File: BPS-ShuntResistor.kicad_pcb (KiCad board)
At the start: 2 copper layers, 40.1 x 35.1 mm, 11 parts, among them J3 Amp_Conn

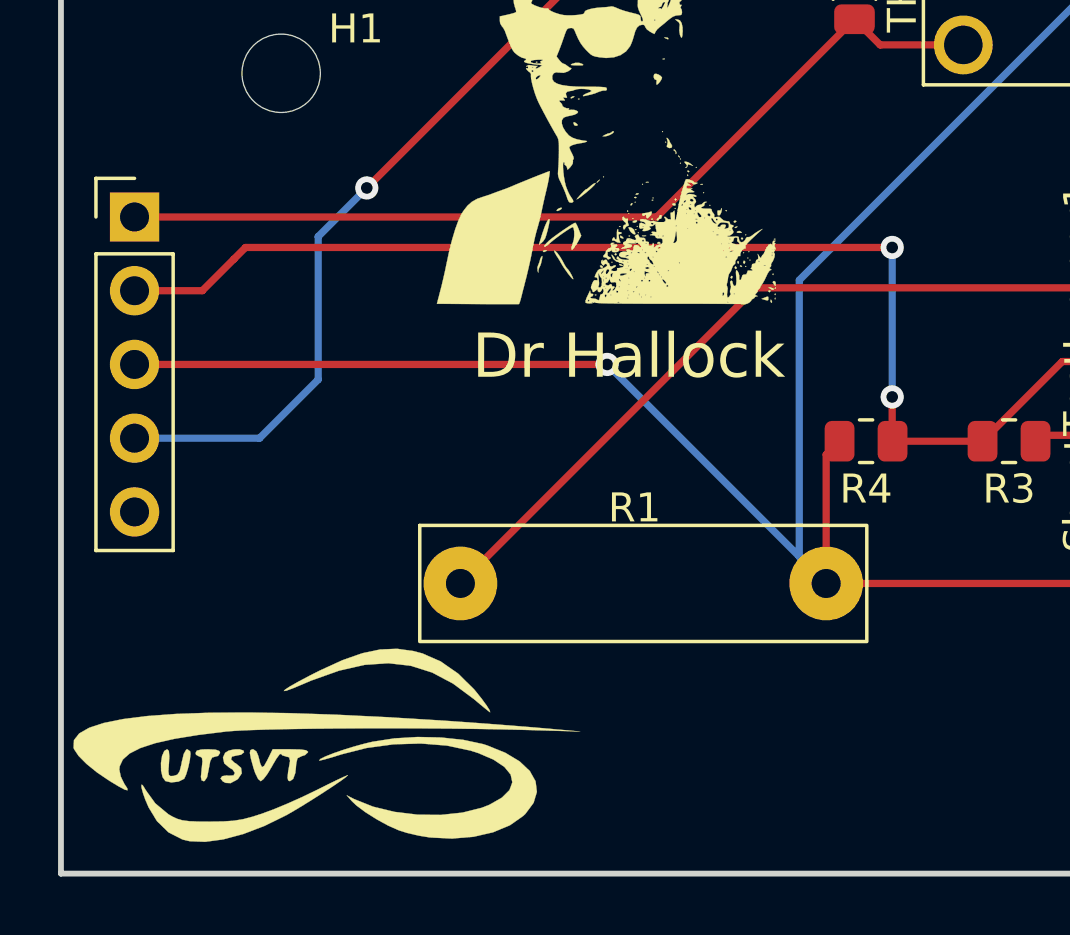
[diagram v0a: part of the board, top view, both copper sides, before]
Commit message: Fixed RSHL/RSHH connectors
Net labels were in wrong spot on circuit
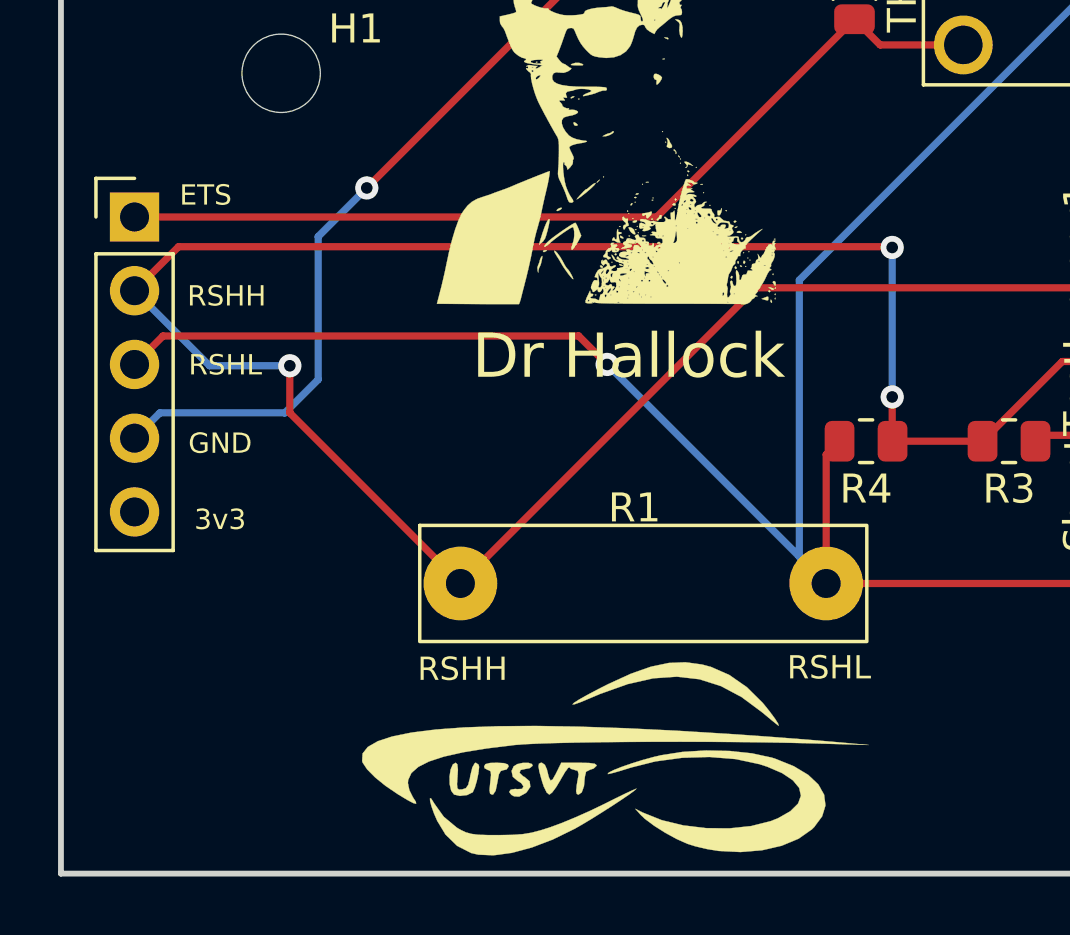
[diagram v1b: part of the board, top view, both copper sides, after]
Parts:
- moved LOGO1 9.95 mm to (127.3, 108.8)
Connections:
- J3 pad 2: RSHH -> Net-(J3-Pad2)
- R1 pad 1: Net-(R1-Pad1) -> RSHH
- R3 pad 2: RSHH -> Net-(J3-Pad2)
- R4 pad 1: RSHH -> Net-(J3-Pad2)
- ShuntTestJumper1 pad 2: Net-(R1-Pad1) -> RSHH
- ShuntTestJumper1 pad 3: RSHH -> Net-(J3-Pad2)
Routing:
- net Net-(J3-Pad2): track 0.00 -> 55.9 mm, vias 0 -> 2
- net Net-(R1-Pad1): track 28.1 -> 0.00 mm
- net RSHH: track 55.9 -> 44.4 mm, vias 2 -> 1
- net RSHL: track 71.7 -> 72.5 mm
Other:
- board text added: "3v3"
- board text added: "ETS"
- board text added: "GND"
- board text added: "RSHH"
- board text added: "RSHL"
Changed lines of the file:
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@@
   (net 5 "+3V3")
   (net 6 "/TestIn")
-  (net 7 "Net-(R1-Pad1)")
+  (net 7 "Net-(J3-Pad2)")
   (net 8 "unconnected-(ShuntTestJumper1-Pad1)")
   (footprint "Connector_PinHeader_2.54mm:PinHeader_1x05_P2.54mm_Vertical" (layer "F.Cu")
@@
   )
   (footprint "UTSVT_Special:UTSVT_Logo_Symbol" (layer "F.Cu")
-    (at 117.359054 108.285857)
+    (at 127.3 108.75)
     (property "Sheetfile" "BPS-ShuntResistor.kicad_sch")
     (property "Sheetname" "")
@@
       (net 6 "/TestIn") (pintype "passive"))
     (pad "2" smd roundrect (at 0.9125 0 180) (size 1.025 1.4) (layers "F.Cu" "F.Paste" "F.Mask") (roundrect_rratio 0.243902439)
-      (net 2 "RSHH") (pintype "passive"))
+      (net 7 "Net-(J3-Pad2)") (pintype "passive"))
     (model "${KICAD6_3DMODEL_DIR}/Resistor_SMD.3dshapes/R_0805_2012Metric.wrl"
       (offset (xyz 0 0 0))
@@
       (net 8 "unconnected-(ShuntTestJumper1-Pad1)") (pinfunction "Pin_1") (pintype "passive+no_connect"))
     (pad "2" thru_hole oval (at 0 2.54) (size 1.7 1.7) (drill 1) (layers *.Cu *.Mask)
-      (net 7 "Net-(R1-Pad1)") (pinfunction "Pin_2") (pintype "passive"))
+      (net 2 "RSHH") (pinfunction "Pin_2") (pintype "passive"))
     (pad "3" thru_hole oval (at 0 5.08) (size 1.7 1.7) (drill 1) (layers *.Cu *.Mask)
-      (net 2 "RSHH") (pinfunction "Pin_3") (pintype "passive"))
+      (net 7 "Net-(J3-Pad2)") (pinfunction "Pin_3") (pintype "passive"))
     (pad "4" thru_hole oval (at 0 7.62) (size 1.7 1.7) (drill 1) (layers *.Cu *.Mask)
       (net 6 "/TestIn") (pinfunction "Pin_4") (pintype "passive"))
@@
     (fp_line (start 1 0.625) (end -1 0.625) (layer "F.Fab") (width 0.1))
     (pad "1" smd roundrect (at -0.9125 0 180) (size 1.025 1.4) (layers "F.Cu" "F.Paste" "F.Mask") (roundrect_rratio 0.243902439)
-      (net 2 "RSHH") (pintype "passive"))
+      (net 7 "Net-(J3-Pad2)") (pintype "passive"))
     (pad "2" smd roundrect (at 0.9125 0 180) (size 1.025 1.4) (layers "F.Cu" "F.Paste" "F.Mask") (roundrect_rratio 0.243902439)
       (net 3 "RSHL") (pintype "passive"))
@@
       (net 1 "ETS") (pinfunction "Pin_1") (pintype "passive"))
     (pad "2" thru_hole circle (at 3 2) (size 2.028 2.028) (drill 1.328) (layers *.Cu *.Mask)
-      (net 2 "RSHH") (pinfunction "Pin_2") (pintype "passive"))
+      (net 7 "Net-(J3-Pad2)") (pinfunction "Pin_2") (pintype "passive"))
     (pad "3" thru_hole circle (at 3 -1.548) (size 2.028 2.028) (drill 1.328) (layers *.Cu *.Mask)
       (net 3 "RSHL") (pinfunction "Pin_3") (pintype "passive"))
@@
     (fp_rect (start -7.4 -2) (end 8 2) (layer "F.SilkS") (width 0.12) (fill none))
     (pad "1" thru_hole circle (at -6 0) (size 2.54 2.54) (drill 1) (layers *.Cu *.Mask)
-      (net 7 "Net-(R1-Pad1)") (pintype "passive"))
+      (net 2 "RSHH") (pintype "passive"))
     (pad "2" thru_hole circle (at 6.6 0) (size 2.54 2.54) (drill 1) (layers *.Cu *.Mask)
       (net 3 "RSHL") (pintype "passive"))
   )
   (gr_rect (start 108.49 77.47) (end 148.59 112.57) (layer "Edge.Cuts") (width 0.2) (fill none))
+  (gr_text "RSHL" (at 134.95 105.475) (layer "F.SilkS")
+    (effects (font (size 0.8 0.8) (thickness 0.2)))
+  )
+  (gr_text "3v3" (at 113.975 100.375) (layer "F.SilkS")
+    (effects (font (size 0.7 0.7) (thickness 0.175)))
+  )
+  (gr_text "ETS" (at 113.475 89.2) (layer "F.SilkS")
+    (effects (font (size 0.7 0.7) (thickness 0.175)))
+  )
+  (gr_text "RSHL" (at 114.15 95.05) (layer "F.SilkS")
+    (effects (font (size 0.7 0.7) (thickness 0.175)))
+  )
+  (gr_text "GND" (at 113.975 97.75) (layer "F.SilkS")
+    (effects (font (size 0.7 0.7) (thickness 0.175)))
+  )
+  (gr_text "RSHH\n" (at 122.325 105.525) (layer "F.SilkS")
+    (effects (font (size 0.8 0.8) (thickness 0.2)))
+  )
+  (gr_text "RSHH" (at 114.2 92.675) (layer "F.SilkS")
+    (effects (font (size 0.7 0.7) (thickness 0.175)))
+  )
   (gr_text "The connectors are aligned according to the\nBPS/Amperes board measurements" (at 90.925 65.175) (layer "Cmts.User")
     (effects (font (size 1.5 1.5) (thickness 0.3)))
@@
   (segment (start 136.7105 84.023) (end 135.825 83.1375) (width 0.25) (layer "F.Cu") (net 1))
   (segment (start 129.0125 89.95) (end 135.825 83.1375) (width 0.25) (layer "F.Cu") (net 1))
-  (segment (start 140.2375 97.675) (end 137.1375 97.675) (width 0.25) (layer "F.Cu") (net 2))
-  (segment (start 111.025 92.49) (end 113.36 92.49) (width 0.25) (layer "F.Cu") (net 2))
-  (segment (start 137.125 96.15) (end 137.125 97.6625) (width 0.25) (layer "F.Cu") (net 2))
-  (segment (start 114.85 91) (end 137.125 91) (width 0.25) (layer "F.Cu") (net 2))
-  (segment (start 140.2375 97.675) (end 142.9825 94.93) (width 0.25) (layer "F.Cu") (net 2))
-  (segment (start 113.36 92.49) (end 114.45 91.4) (width 0.25) (layer "F.Cu") (net 2))
-  (segment (start 114.45 91.4) (end 114.85 91) (width 0.25) (layer "F.Cu") (net 2))
-  (segment (start 142.9825 94.93) (end 146.1 94.93) (width 0.25) (layer "F.Cu") (net 2))
-  (segment (start 137.125 97.6625) (end 137.1375 97.675) (width 0.25) (layer "F.Cu") (net 2))
-  (via (at 137.125 96.15) (size 0.8) (drill 0.4) (layers "F.Cu" "B.Cu") (net 2))
-  (via (at 137.125 91) (size 0.8) (drill 0.4) (layers "F.Cu" "B.Cu") (net 2))
-  (segment (start 137.125 91) (end 137.125 96.15) (width 0.25) (layer "B.Cu") (net 2))
-  (segment (start 145.575 84.023) (end 144.025 85.573) (width 0.25) (layer "B.Cu") (net 2))
-  (segment (start 144.025 92.855) (end 146.1 94.93) (width 0.25) (layer "B.Cu") (net 2))
-  (segment (start 144.025 85.573) (end 144.025 92.855) (width 0.25) (layer "B.Cu") (net 2))
+  (segment (start 122.25 102.575) (end 116.375 96.7) (width 0.25) (layer "F.Cu") (net 2))
+  (segment (start 116.375 96.7) (end 116.375 95.075) (width 0.25) (layer "F.Cu") (net 2))
+  (segment (start 146.1 92.39) (end 132.435 92.39) (width 0.25) (layer "F.Cu") (net 2))
+  (segment (start 132.435 92.39) (end 122.25 102.575) (width 0.25) (layer "F.Cu") (net 2))
+  (via (at 116.375 95.075) (size 0.8) (drill 0.4) (layers "F.Cu" "B.Cu") (net 2))
+  (segment (start 113.61 95.075) (end 111.025 92.49) (width 0.25) (layer "B.Cu") (net 2))
+  (segment (start 116.375 95.075) (end 113.61 95.075) (width 0.25) (layer "B.Cu") (net 2))
+  (segment (start 111.025 95.03) (end 112.005 94.05) (width 0.25) (layer "F.Cu") (net 3))
   (segment (start 134.85 98.1375) (end 134.85 102.575) (width 0.25) (layer "F.Cu") (net 3))
+  (segment (start 126.325 94.05) (end 127.305 95.03) (width 0.25) (layer "F.Cu") (net 3))
   (segment (start 146.1 100.01) (end 143.535 102.575) (width 0.25) (layer "F.Cu") (net 3))
+  (segment (start 112.005 94.05) (end 126.325 94.05) (width 0.25) (layer "F.Cu") (net 3))
   (segment (start 143.535 102.575) (end 134.85 102.575) (width 0.25) (layer "F.Cu") (net 3))
   (segment (start 135.3125 97.675) (end 134.85 98.1375) (width 0.25) (layer "F.Cu") (net 3))
-  (segment (start 111.025 95.03) (end 127.305 95.03) (width 0.25) (layer "F.Cu") (net 3))
   (via (at 127.305 95.03) (size 0.8) (drill 0.4) (layers "F.Cu" "B.Cu") (net 3))
   (segment (start 145.575 80.475) (end 133.925 92.125) (width 0.25) (layer "B.Cu") (net 3))
@@
   (segment (start 136.6625 80.475) (end 135.825 81.3125) (width 0.25) (layer "F.Cu") (net 4))
   (via (at 119.025 88.95) (size 0.8) (drill 0.4) (layers "F.Cu" "B.Cu") (net 4))
-  (segment (start 115.325 97.575) (end 115.32 97.57) (width 0.25) (layer "B.Cu") (net 4))
-  (segment (start 115.32 97.57) (end 111.025 97.57) (width 0.25) (layer "B.Cu") (net 4))
-  (segment (start 117.35 95.55) (end 115.325 97.575) (width 0.25) (layer "B.Cu") (net 4))
-  (segment (start 117.35 90.625) (end 117.35 95.55) (width 0.25) (layer "B.Cu") (net 4))
   (segment (start 119.025 88.95) (end 117.35 90.625) (width 0.25) (layer "B.Cu") (net 4))
+  (segment (start 117.35 90.625) (end 117.35 95.55) (width 0.25) (layer "B.Cu") (net 4))
+  (segment (start 117.35 95.55) (end 116.2 96.7) (width 0.25) (layer "B.Cu") (net 4))
+  (segment (start 111.895 96.7) (end 111.025 97.57) (width 0.25) (layer "B.Cu") (net 4))
+  (segment (start 116.2 96.7) (end 111.895 96.7) (width 0.25) (layer "B.Cu") (net 4))
   (segment (start 142.2675 97.47) (end 146.1 97.47) (width 0.25) (layer "F.Cu") (net 6))
   (segment (start 142.0625 97.675) (end 142.2675 97.47) (width 0.25) (layer "F.Cu") (net 6))
-  (segment (start 146.1 92.39) (end 132.435 92.39) (width 0.25) (layer "F.Cu") (net 7))
-  (segment (start 132.435 92.39) (end 122.25 102.575) (width 0.25) (layer "F.Cu") (net 7))
+  (segment (start 140.2375 97.675) (end 137.1375 97.675) (width 0.25) (layer "F.Cu") (net 7))
+  (segment (start 137.125 96.15) (end 137.125 97.6625) (width 0.25) (layer "F.Cu") (net 7))
+  (segment (start 112.54 90.975) (end 137.1 90.975) (width 0.25) (layer "F.Cu") (net 7))
+  (segment (start 140.2375 97.675) (end 142.9825 94.93) (width 0.25) (layer "F.Cu") (net 7))
+  (segment (start 142.9825 94.93) (end 146.1 94.93) (width 0.25) (layer "F.Cu") (net 7))
+  (segment (start 137.1 90.975) (end 137.125 91) (width 0.25) (layer "F.Cu") (net 7))
+  (segment (start 111.025 92.49) (end 112.54 90.975) (width 0.25) (layer "F.Cu") (net 7))
+  (segment (start 137.125 97.6625) (end 137.1375 97.675) (width 0.25) (layer "F.Cu") (net 7))
+  (via (at 137.125 96.15) (size 0.8) (drill 0.4) (layers "F.Cu" "B.Cu") (net 7))
+  (via (at 137.125 91) (size 0.8) (drill 0.4) (layers "F.Cu" "B.Cu") (net 7))
+  (segment (start 137.125 91) (end 137.125 96.15) (width 0.25) (layer "B.Cu") (net 7))
+  (segment (start 145.575 84.023) (end 144.025 85.573) (width 0.25) (layer "B.Cu") (net 7))
+  (segment (start 144.025 92.855) (end 146.1 94.93) (width 0.25) (layer "B.Cu") (net 7))
+  (segment (start 144.025 85.573) (end 144.025 92.855) (width 0.25) (layer "B.Cu") (net 7))
 )

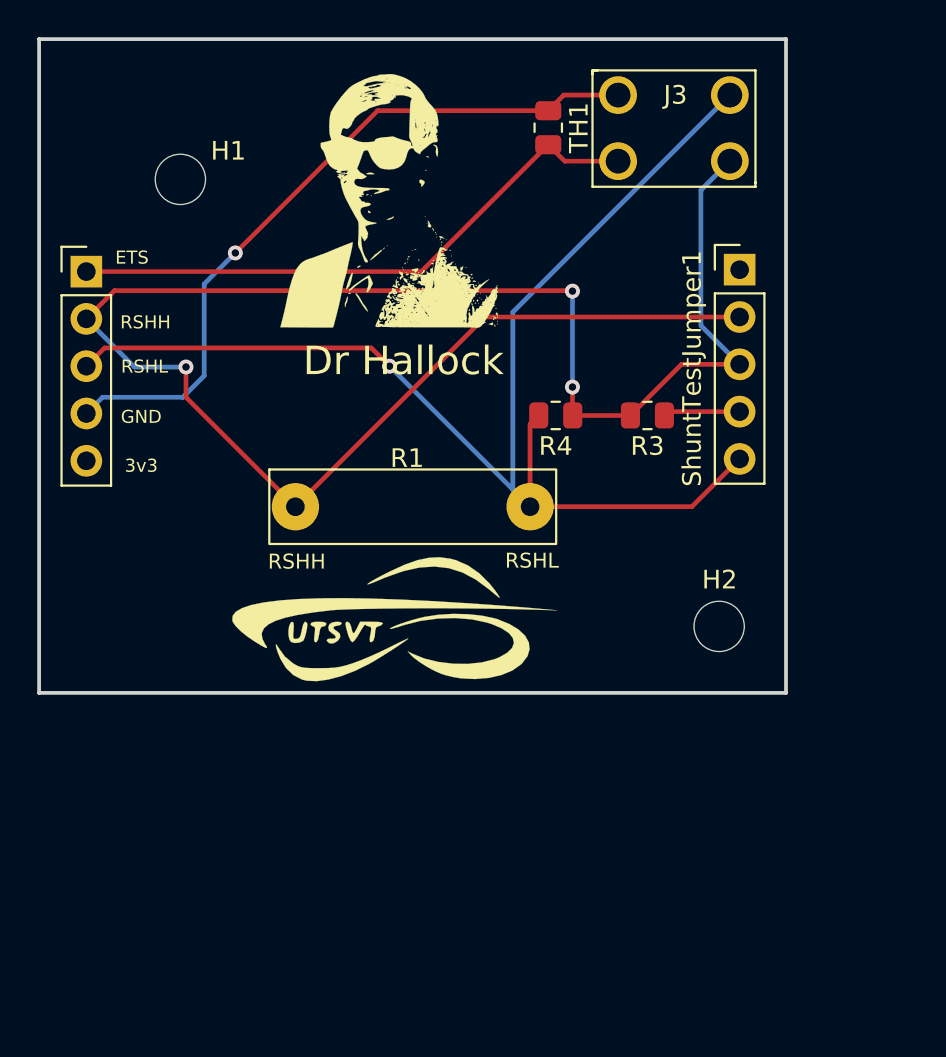
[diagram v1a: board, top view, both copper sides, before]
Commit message: moved to exact same positions as tianda
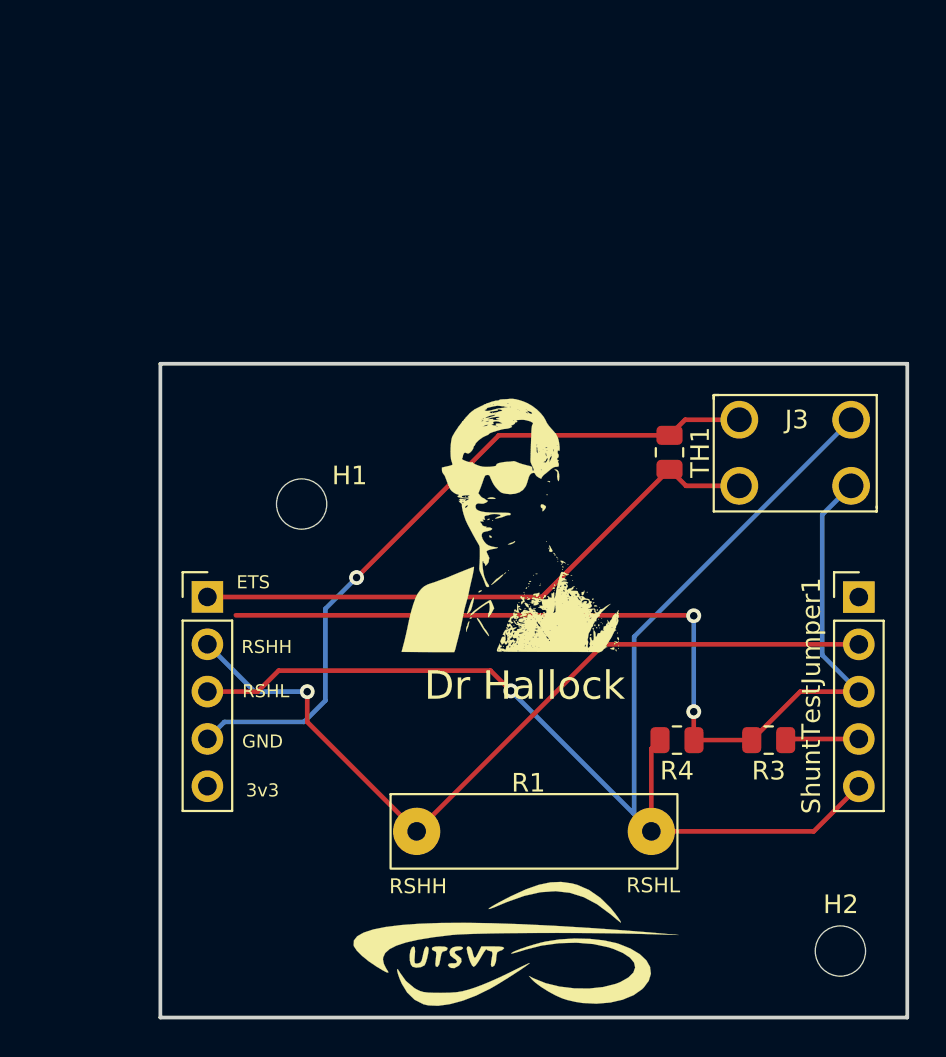
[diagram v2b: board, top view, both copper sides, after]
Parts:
- moved ShuntTestJumper1 18.7 mm to (152.5, 107.4)
- moved CurrentBoardConn1 18.6 mm to (117.5, 107.4)
- moved J3 18.6 mm to (149.1, 99.5)
- moved R4 18.6 mm to (142.7, 115.1)
- moved TH1 18.6 mm to (142.3, 99.7)
- moved LOGO1 18.6 mm to (133.8, 126.2)
- moved LOGO2 18.6 mm to (133.3, 103.4)
- moved H1 18.6 mm to (122.6, 102.4)
- moved H2 18.6 mm to (151.5, 126.4)
- moved R3 18.6 mm to (147.7, 115.1)
- moved R1 18.6 mm to (134.8, 120.0)
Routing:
- net Net-(J3-Pad2): track 55.9 -> 53.7 mm
